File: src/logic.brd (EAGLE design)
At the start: 36 x 73.5 mm, 97 parts, among them CON1 CON-4P-TABS-JST_GH-RA, CON11 PINHEAD_1X04-2, CON12 PINHEAD_1X04-2, CON2 PINHEAD_1X04-2.54, CON3 PINHEAD_2X04-PLS-2, CON4 PINHEAD_2X03-PTH-2, CON5 PINHEAD_2X03-PTH-2, IC1 STM32F105RCT6, IC10 LM75-TSSOP8, IC101 LM5017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

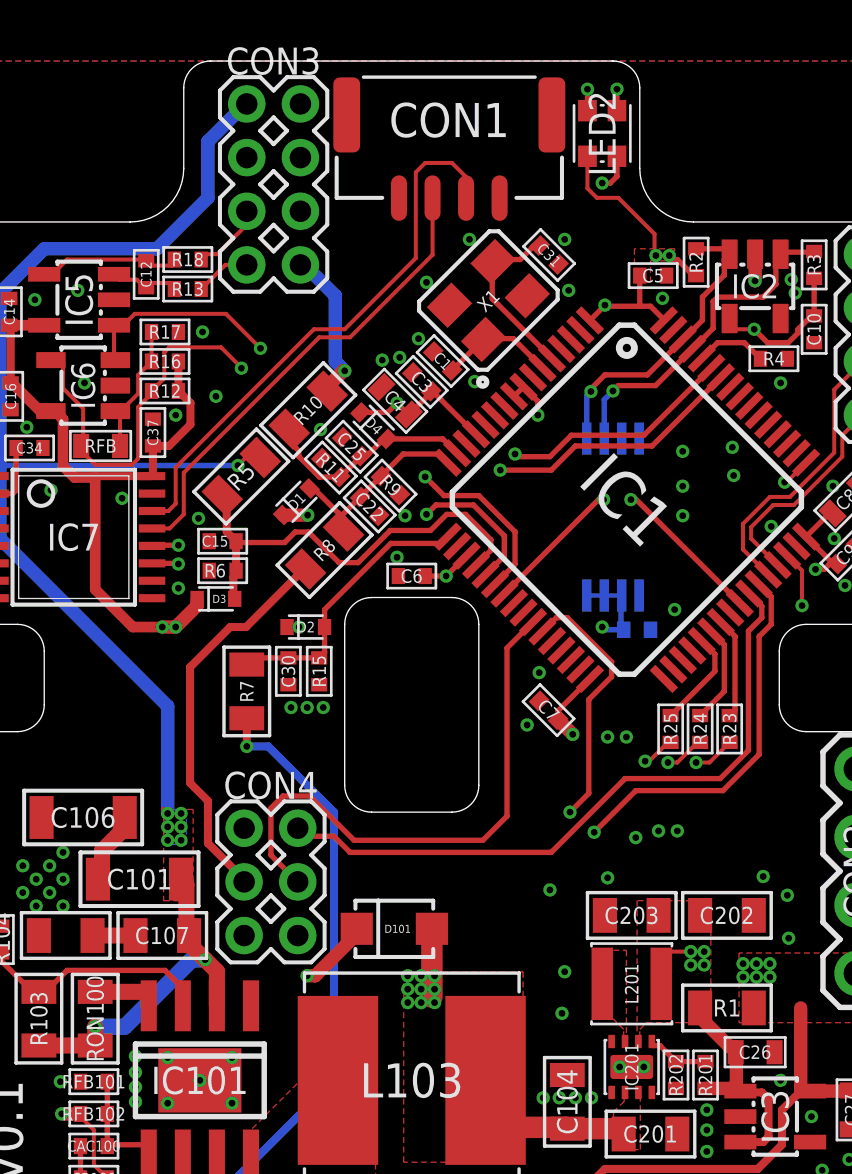
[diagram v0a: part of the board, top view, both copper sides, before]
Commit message: RC PWM updated
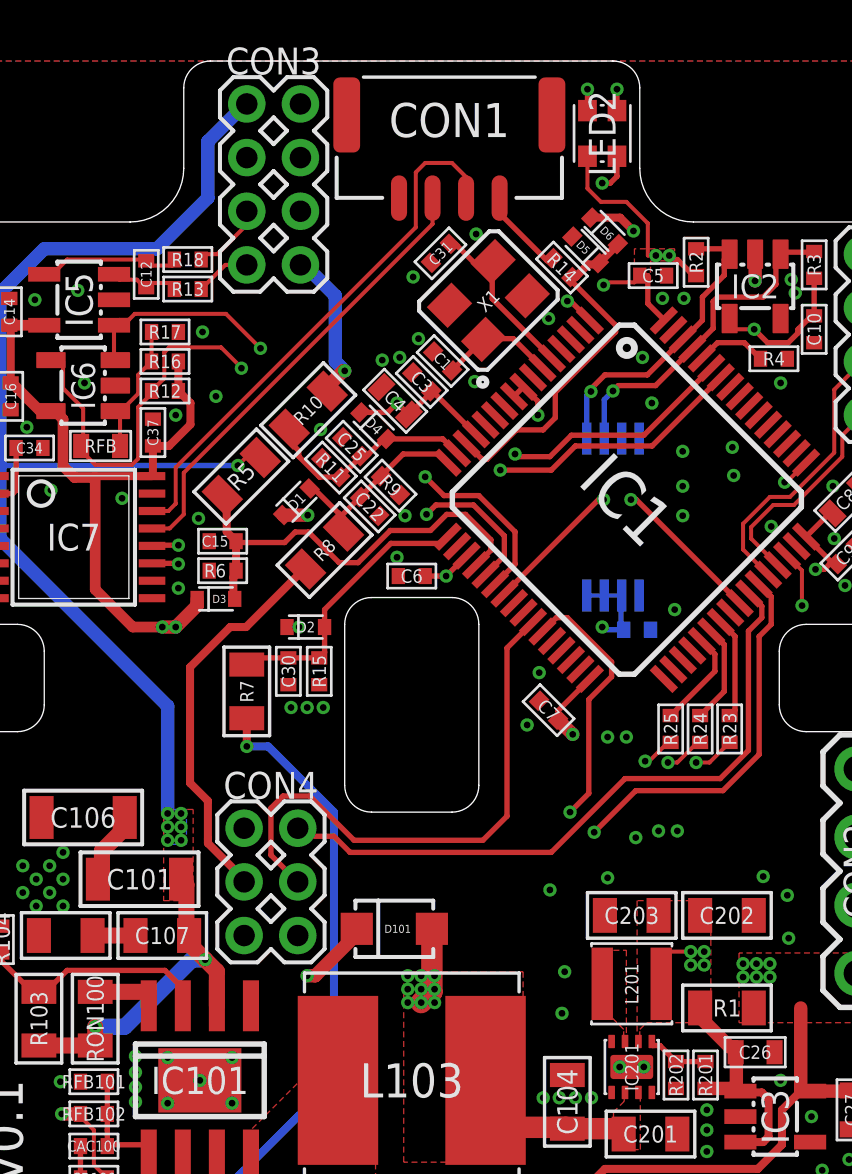
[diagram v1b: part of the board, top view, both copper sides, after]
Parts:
- added D5, D6: BAT54KFILM, Diodes:SOD523
- added R14: 200R, rc:R0402
- C1, C31: value 18pF -> 9pF
- C15, C22, C25, C30: value 5600pF -> 4700pF
- R10, R7, R8: value 47K -> 51K
- R11, R15, R9: value 1K5 -> 1K8
- moved C31 4.05 mm to (1.07, 72.8), turned to 45 degrees
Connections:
- removed net RCPWM: CON1.1
- removed net TSENS_OS: IC1.56
- new net N$2: CON1.1, R14.1
- net GND: now also D5.A
- net RC_PWM: now also D5.C, D6.A, R14.2
- net VDD_5V: now also D6.C
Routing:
- net RC_PWM: track 0.00 -> 13.3 mm
- net VDD_5V: track 50.9 -> 61.6 mm, vias 4 -> 5
- net N$2: track 0.00 -> 3.31 mm
- net VDD_3V3: track 203.1 -> 205.4 mm, vias 22 -> 23
- net N$7: track 31.7 -> 32.8 mm
- net N$6: track 26.3 -> 27.3 mm
- net N$26: track 29.6 -> 30.6 mm
- net N$30: track 20.7 -> 20.1 mm
- net N$29: track 17.7 -> 17.0 mm
- net GND: vias 90 -> 92

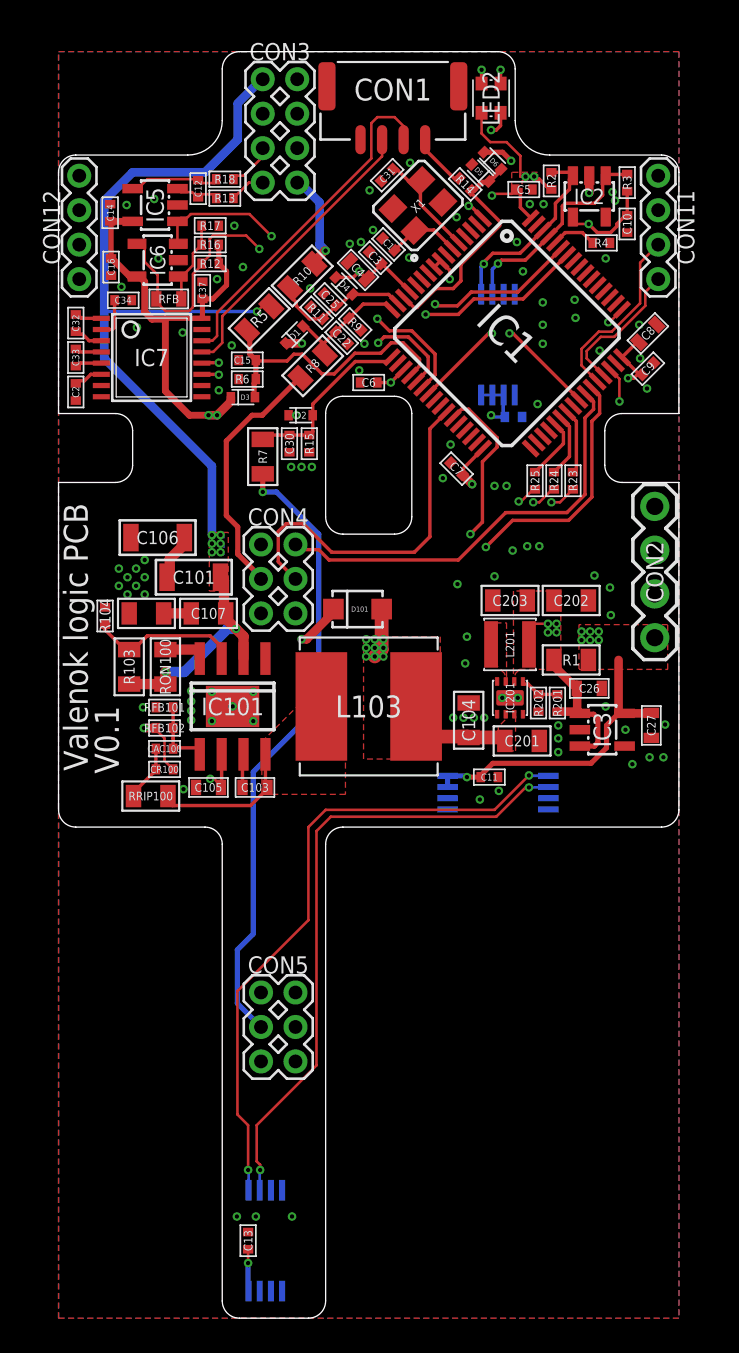
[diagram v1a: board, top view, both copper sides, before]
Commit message: Crystal attributes update
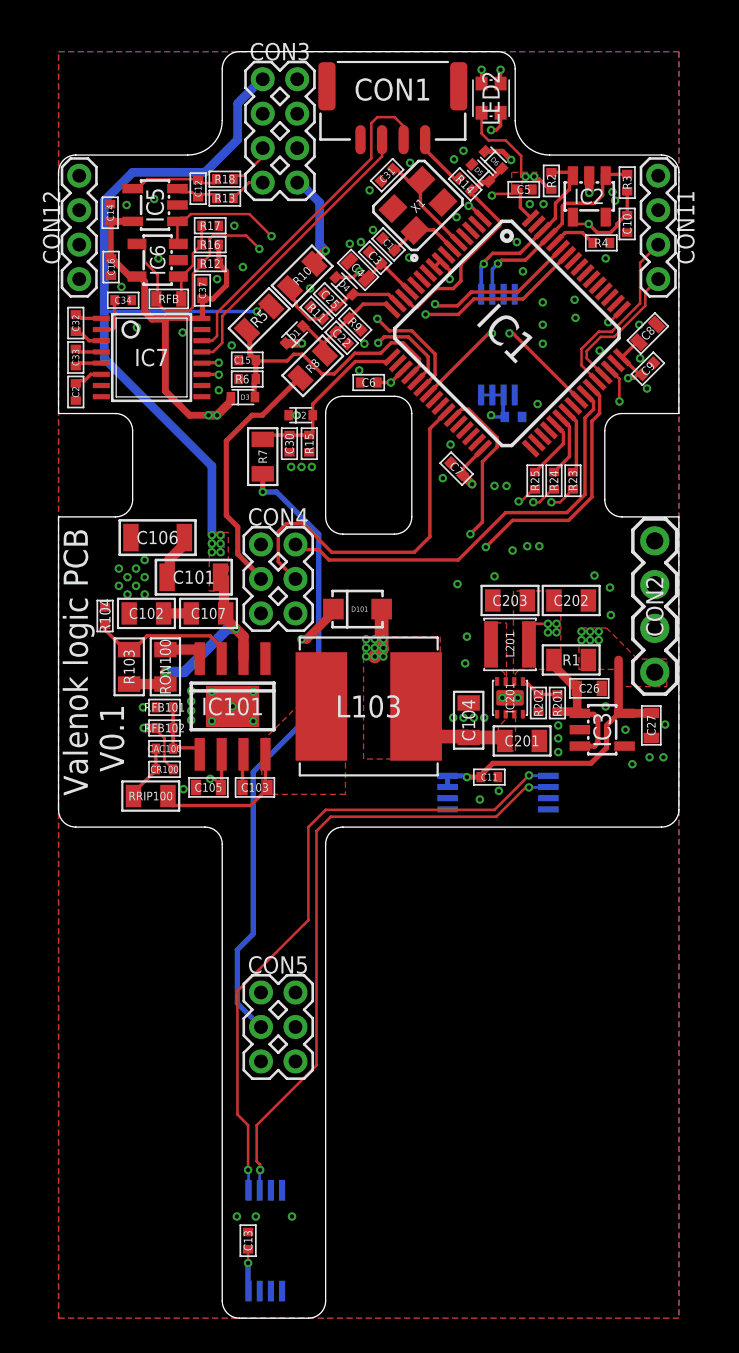
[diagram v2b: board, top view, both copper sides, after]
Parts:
- RFB102: value 3K -> 10K
- moved CON2 2.00 mm to (16.6, 47.8)
- moved D6 0.07 mm to (7.24, 73.7)
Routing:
- net SWCLK: track 16.4 -> 18.4 mm
- net SWDIO: track 11.5 -> 13.4 mm
- net GND: vias 92 -> 94
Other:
- outline, holes or cut-outs redrawn

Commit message: Massive routing update
InterPCB connectors between Cap PCB and power PCB replaced with bigger ones
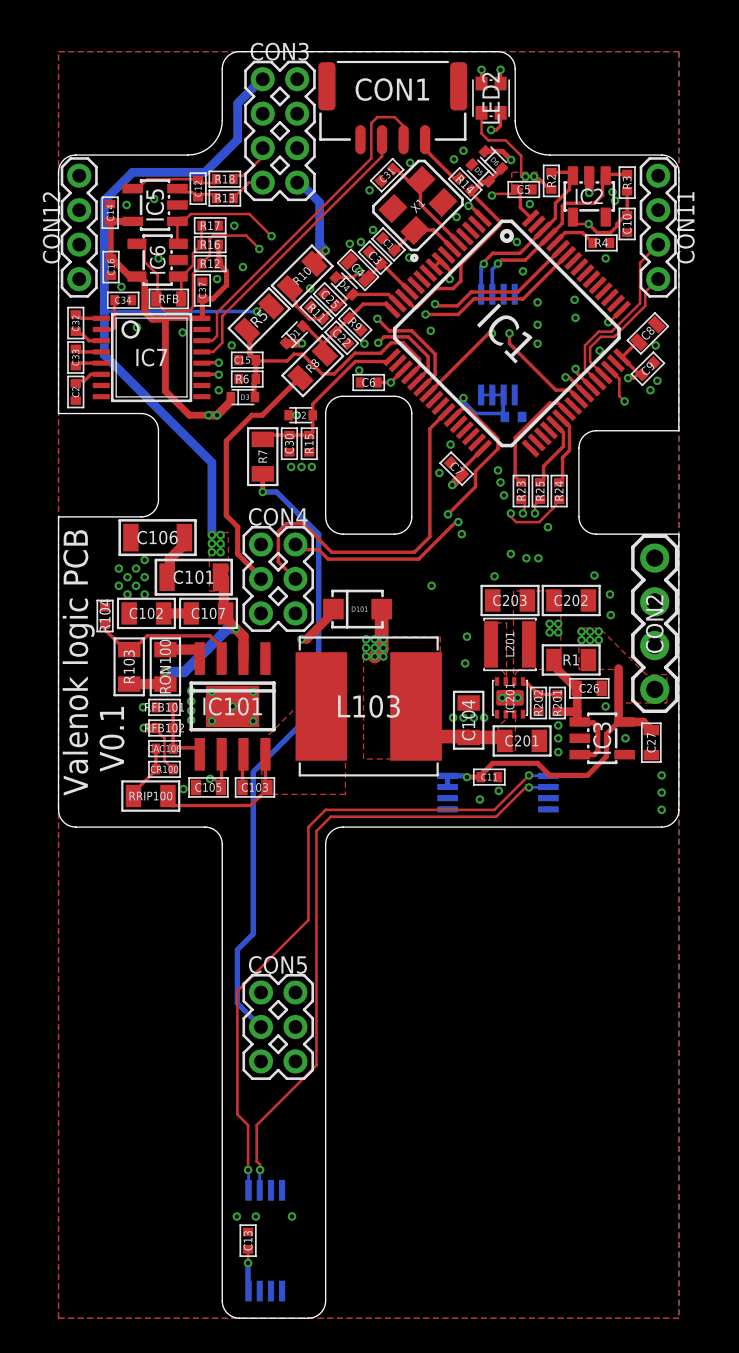
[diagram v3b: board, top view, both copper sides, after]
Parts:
- moved R23 3.06 mm to (8.85, 54.5)
- moved C27 1.00 mm to (16.4, 39.9)
- moved CON2 1.00 mm to (16.6, 46.8)
- moved R24 0.67 mm to (11.1, 54.5)
- moved R25 0.67 mm to (9.95, 54.5)
- moved IC3 0.50 mm to (13.6, 40.1)
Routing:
- net VDD_5V: track 61.6 -> 57.4 mm
- net SWDIO: track 13.4 -> 16.9 mm
- net SWCLK: track 18.4 -> 21.7 mm
- net N$18: track 3.79 -> 6.80 mm
- net N$7: track 32.8 -> 30.0 mm
- net N$26: track 30.6 -> 33.3 mm
- net VDD_3V3: track 205.4 -> 207.6 mm
- net FET_B_H: track 25.0 -> 23.2 mm, vias 0 -> 2
- net FET_C_H: track 44.5 -> 44.4 mm, vias 1 -> 2
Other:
- outline, holes or cut-outs redrawn

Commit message: DC-DC design notes update
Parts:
- moved C2 0.10 mm to (-17.0, 60.4)
- moved C33 0.10 mm to (-17.0, 62.4)
- moved C32 0.10 mm to (-17.0, 64.3)
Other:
- outline, holes or cut-outs redrawn

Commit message: Notes added
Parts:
- moved C202 0.20 mm to (11.8, 48.4)
- moved C203 0.20 mm to (8.20, 48.4)
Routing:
- net VDC: track 58.6 -> 59.8 mm
- net VDD_3V3: track 207.6 -> 207.0 mm
- net GND: vias 94 -> 116
- added copper zone on layer 2, net VDC
- removed copper zone on layer 16, net VDC
